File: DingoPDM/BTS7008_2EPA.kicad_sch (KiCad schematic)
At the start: 13 parts, among them U17 BTS7008-2EPA

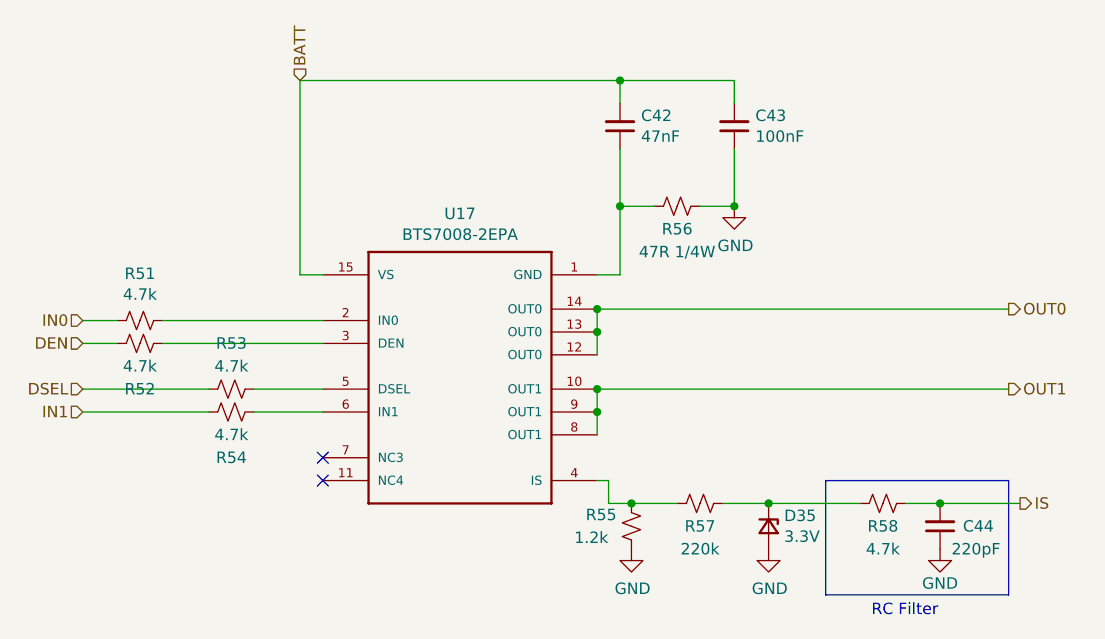
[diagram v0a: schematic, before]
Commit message: Redesigned to a smaller unit
4x high current, 2x med current, 4x low current, 2x digital inputs
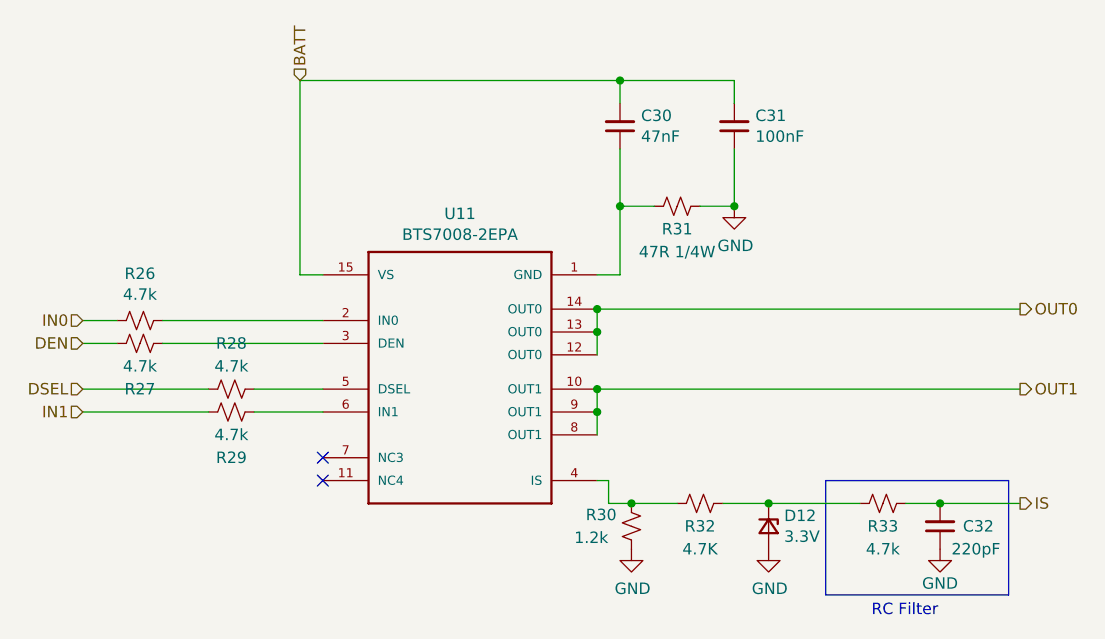
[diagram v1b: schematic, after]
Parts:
- C31: renamed from C43; LCSC (none) -> C49678
- R26: renamed from R51; LCSC (none) -> C17673
- R27: renamed from R52; LCSC (none) -> C17673
- R28: renamed from R53; LCSC (none) -> C17673
- R29: renamed from R54; LCSC (none) -> C17673
- R32: renamed from R57; value 220k -> 4.7K
- R33: renamed from R58; LCSC (none) -> C17673
- U11: renamed from U17; LCSC (none) -> C2150060
- renumbered C42 to C30, C44 to C32, D35 to D12, R55 to R30, R56 to R31

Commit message: Added documentation, finished and cleaned design
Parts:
- C30: LCSC (none) -> C520039
- C32: LCSC (none) -> C576920
- D12: LCSC (none) -> C177016
- R30: LCSC (none) -> C727987
- R31: LCSC (none) -> C2907508
- R32: value 4.7K -> 4.7k; Digi-Key_PN 311-220KARCT-ND -> 311-4.70KCRCT-ND; LCSC (none) -> C17673
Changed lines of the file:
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@@
   (title_block
     (title "Dingo_PDM")
-    (date "2023-04-01")
-    (rev "v5")
+    (date "2023-07-28")
+    (rev "v6")
     (comment 3 "github.com/corygrant")
     (comment 4 "Cory Grant")
@@
       (effects (font (size 1.27 1.27)) hide)
     )
-    (property "LCSC" "" (at 146.05 71.12 0)
+    (property "LCSC" "C520039" (at 146.05 71.12 0)
       (effects (font (size 1.27 1.27)) hide)
     )
@@
       (effects (font (size 1.27 1.27)) hide)
     )
-    (property "LCSC" "" (at 152.4 80.01 0)
+    (property "LCSC" "C2907508" (at 152.4 80.01 0)
       (effects (font (size 1.27 1.27)) hide)
     )
@@
       (effects (font (size 1.27 1.27)) hide)
     )
-    (property "LCSC" "" (at 181.61 115.57 0)
+    (property "LCSC" "C576920" (at 181.61 115.57 0)
       (effects (font (size 1.27 1.27)) hide)
     )
@@
       (effects (font (size 1.27 1.27)) hide)
     )
-    (property "LCSC" "" (at 147.32 115.57 0)
+    (property "LCSC" "C727987" (at 147.32 115.57 0)
       (effects (font (size 1.27 1.27)) hide)
     )
@@
       (effects (font (size 1.27 1.27)))
     )
-    (property "Value" "4.7K" (at 154.94 118.11 90)
+    (property "Value" "4.7k" (at 154.94 118.11 90)
       (effects (font (size 1.27 1.27)))
     )
@@
       (effects (font (size 1.27 1.27)) hide)
     )
-    (property "Digi-Key_PN" "311-220KARCT-ND" (at 154.94 113.03 0)
-      (effects (font (size 1.27 1.27)) hide)
-    )
-    (property "LCSC" "" (at 154.94 113.03 0)
+    (property "Digi-Key_PN" "311-4.70KCRCT-ND" (at 154.94 113.03 0)
+      (effects (font (size 1.27 1.27)) hide)
+    )
+    (property "LCSC" "C17673" (at 154.94 113.03 0)
       (effects (font (size 1.27 1.27)) hide)
     )
@@
       (effects (font (size 1.27 1.27)) hide)
     )
-    (property "LCSC" "" (at 162.56 115.57 0)
-      (effects (font (size 1.27 1.27)) hide)
-    )
+    (property "LCSC" "C177016" (at 162.56 115.57 0)
+      (effects (font (size 1.27 1.27)) hide)
+    )

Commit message: Small edits
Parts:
- R26, R27, R28, R29, R32, R33: value 4.7k -> 4.7K
- R30: value 1.2k -> 1.2K
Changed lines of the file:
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@@
       (effects (font (size 1.27 1.27)))
     )
-    (property "Value" "4.7k" (at 92.71 89.8144 90)
+    (property "Value" "4.7K" (at 92.71 89.8144 90)
       (effects (font (size 1.27 1.27)))
     )
@@
       (effects (font (size 1.27 1.27)))
     )
-    (property "Value" "4.7k" (at 92.71 97.79 90)
+    (property "Value" "4.7K" (at 92.71 97.79 90)
       (effects (font (size 1.27 1.27)))
     )
@@
       (effects (font (size 1.27 1.27)))
     )
-    (property "Value" "4.7k" (at 175.26 118.11 90)
+    (property "Value" "4.7K" (at 175.26 118.11 90)
       (effects (font (size 1.27 1.27)))
     )
@@
       (effects (font (size 1.27 1.27)) (justify left))
     )
-    (property "Value" "1.2k" (at 140.97 116.84 0)
+    (property "Value" "1.2K" (at 140.97 116.84 0)
       (effects (font (size 1.27 1.27)) (justify left))
     )
@@
       (effects (font (size 1.27 1.27)))
     )
-    (property "Value" "4.7k" (at 154.94 118.11 90)
+    (property "Value" "4.7K" (at 154.94 118.11 90)
       (effects (font (size 1.27 1.27)))
     )
@@
       (effects (font (size 1.27 1.27)))
     )
-    (property "Value" "4.7k" (at 102.87 97.79 90)
+    (property "Value" "4.7K" (at 102.87 97.79 90)
       (effects (font (size 1.27 1.27)))
     )
@@
       (effects (font (size 1.27 1.27)))
     )
-    (property "Value" "4.7k" (at 102.87 105.41 90)
-      (effects (font (size 1.27 1.27)))
-    )
+    (property "Value" "4.7K" (at 102.87 105.41 90)
+      (effects (font (size 1.27 1.27)))
+    )

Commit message: Updated JLC zener diode part and batt volt divider
The previous zener diode had too low of a breakdown zener voltage.
The previous voltage divider was also too high of an output voltage, swapped R2 to lower the max voltage to well below the breakdown zener voltage
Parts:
- D12: LCSC C177016 -> C426855
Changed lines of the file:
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@@
       (effects (font (size 1.27 1.27)) hide)
     )
-    (property "LCSC" "C177016" (at 162.56 115.57 0)
+    (property "LCSC" "C426855" (at 162.56 115.57 0)
       (effects (font (size 1.27 1.27)) hide)
     )

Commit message: Update JLC part numbers for in stock ones
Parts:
- R30: LCSC C727987 -> C2933520
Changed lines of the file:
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@@
       (effects (font (size 1.27 1.27)) hide)
     )
-    (property "LCSC" "C727987" (at 147.32 115.57 0)
+    (property "LCSC" "C2933520" (at 147.32 115.57 0)
       (effects (font (size 1.27 1.27)) hide)
     )
